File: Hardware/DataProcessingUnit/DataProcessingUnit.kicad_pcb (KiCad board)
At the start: 2 copper layers, 85 x 60 mm, 49 parts, among them J1 USB_B_Micro, J4 Conn_01x07, Q2 BC847, SW1 SW_Push, U2 LD1117S33TR, U3 STM32F103RBTx, Y1 32,768kHz, Y2 Crystal

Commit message: corections after hw sw integration
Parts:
- C11, C12: value 6p8 -> 10p
- C13, C14: value 6p8 -> 22p
- C9: value 100n -> 1u
- R13, R14: value TBD -> 0R
- Y1: value 32,768kHz -> 32,768kHz /12.5p
- Y2: value Crystal -> 8M
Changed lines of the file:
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@@
 			(psa4output no)
 			(plot_black_and_white yes)
-			(plotinvisibletext no)
 			(sketchpadsonfab no)
 			(plotpadnumbers no)
@@
 			)
 		)
-		(property "Value" "32,768kHz"
+		(property "Value" "32,768kHz /12.5p"
 			(at 0 2.000001 45)
 			(layer "F.Fab")
@@
 			)
 		)
-		(property "Value" "6p8"
+		(property "Value" "10p"
 			(at 0 1.679999 135)
 			(layer "F.Fab")
@@
 			)
 		)
-		(property "Value" "TBD"
+		(property "Value" "0R"
 			(at 0 1.65 45)
 			(layer "F.Fab")
@@
 			)
 		)
-		(property "Value" "TBD"
+		(property "Value" "0R"
 			(at 0 1.65 45)
 			(layer "F.Fab")
@@
 			)
 		)
-		(property "Value" "Crystal"
+		(property "Value" "8M"
 			(at 0 3.55 135)
 			(layer "F.Fab")
@@
 			)
 		)
-		(property "Value" "6p8"
+		(property "Value" "10p"
 			(at 0 1.679999 135)
 			(layer "F.Fab")
@@
 			)
 		)
-		(property "Value" "6p8"
+		(property "Value" "22p"
 			(at 0 1.679999 45)
 			(layer "F.Fab")
@@
 				(keep_text_aligned yes)
 			)
-			(gr_text "39,54"
+			(gr_text "39.54"
 				(at 192.27 129.15 0)
 				(layer "F.Fab")
@@
 				(keep_text_aligned yes)
 			)
-			(gr_text "79,5"
+			(gr_text "79.5"
 				(at 172.29 104.65 0)
 				(layer "User.1")
@@
 			)
 		)
-		(property "Value" "6p8"
+		(property "Value" "22p"
 			(at 0 1.679999 45)
 			(layer "F.Fab")
@@
 			)
 		)
-		(property "Value" "100n"
+		(property "Value" "1u"
 			(at 0 1.68 0)
 			(layer "F.Fab")
@@
 			(keep_text_aligned yes)
 		)
-		(gr_text "85,0000 mm"
+		(gr_text "85.0000 mm"
 			(at 172.5 126.35 0)
 			(layer "Cmts.User")
@@
 			(keep_text_aligned yes)
 		)
-		(gr_text "100,0000 mm"
+		(gr_text "100.0000 mm"
 			(at 124.6 70 90)
 			(layer "Cmts.User")
@@
 			(keep_text_aligned yes)
 		)
-		(gr_text "60,0000 mm"
+		(gr_text "60.0000 mm"
 			(at 223.85 90 90)
 			(layer "Cmts.User")
@@
 			(keep_text_aligned yes)
 		)
-		(gr_text "100,0000 mm"
+		(gr_text "100.0000 mm"
 			(at 180 133.85 0)
 			(layer "Cmts.User")
@@
 			(keep_text_aligned yes)
 		)
-		(gr_text "42,5000 mm"
+		(gr_text "42.5000 mm"
 			(at 151.25 122.2 0)
 			(layer "Cmts.User")

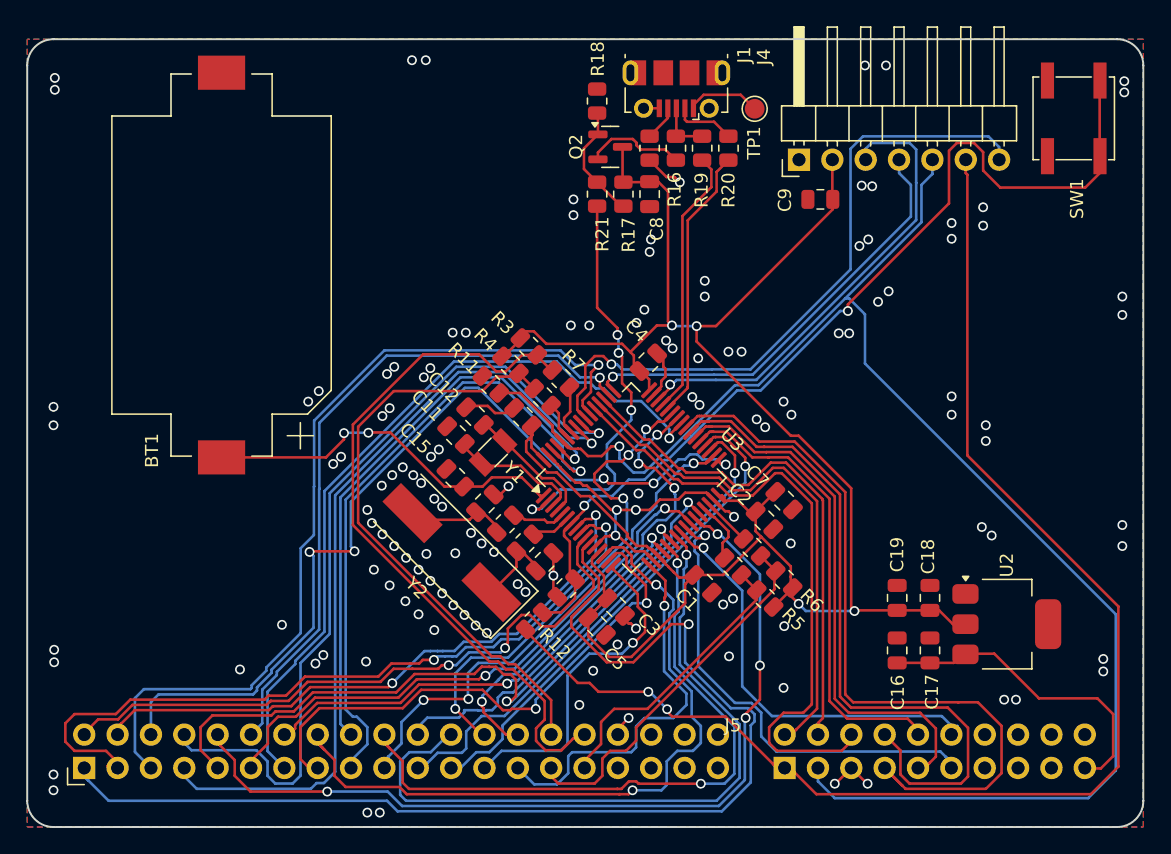
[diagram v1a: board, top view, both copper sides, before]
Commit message: rework CI, make PCB smaller
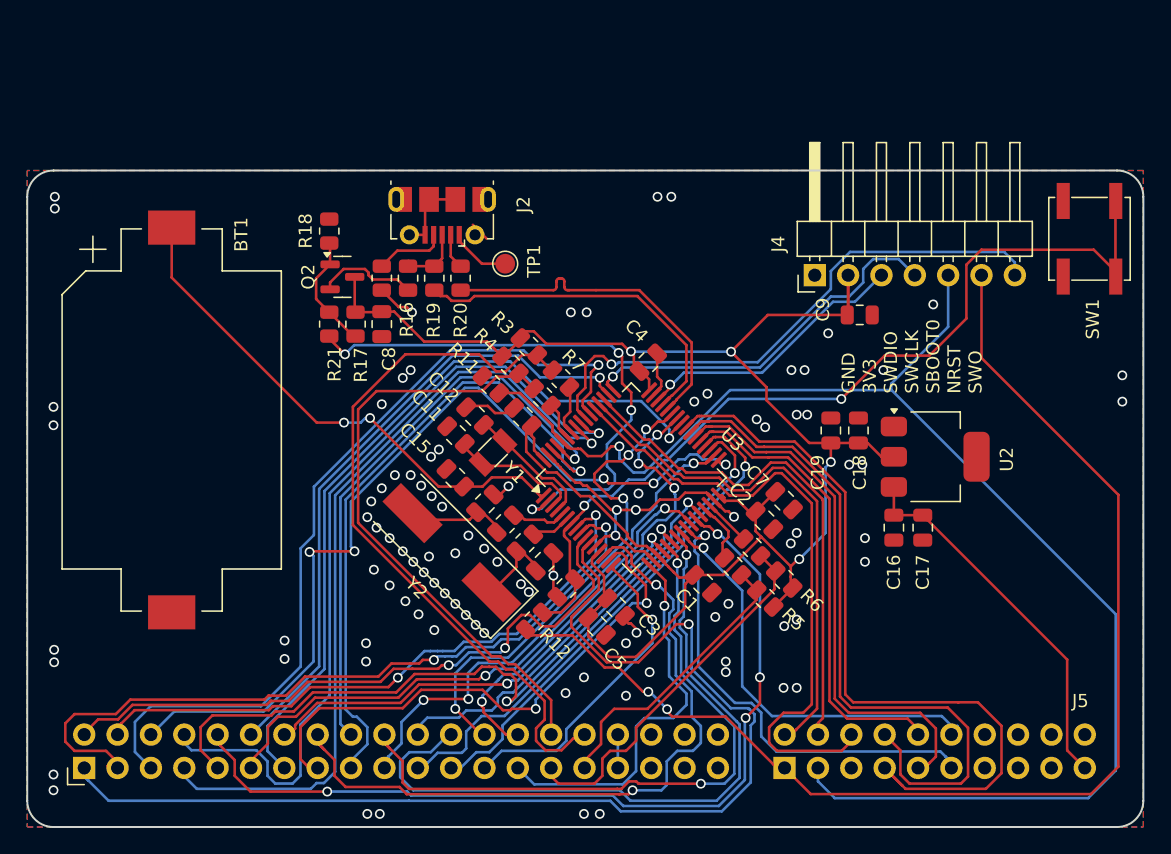
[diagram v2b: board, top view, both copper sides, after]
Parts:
- removed J1: USB_B_Micro, Connector_USB:USB_Micro-B_Molex-105017-0001
- added J2: USB_B_Micro, HardwareDataLogger:USB_Micro-B_Molex-105017-0001_Extra_Mechanical_Pads, F.Cu at (162.0, 75.7)
- C11, C12: value 10p -> 6p8
- C13, C14: value 22p -> 6p8
- C9: value 1u -> 100n
- R13, R14: value 0R -> TBD
- Y1: value 32,768kHz /12.5p -> 32,768kHz
- Y2: value 8M -> Crystal
- moved C8 22.7 mm to (157.0, 81.7)
- moved R15 22.7 mm to (157.0, 78.2)
- moved R16 22.7 mm to (159.0, 78.2)
- moved R17 22.7 mm to (155.0, 81.7)
- moved R19 22.7 mm to (161.0, 78.2)
- moved R20 22.7 mm to (163.0, 78.2)
- moved R21 22.7 mm to (153.0, 81.7)
- moved Q2 22.7 mm to (154.0, 78.1)
- moved R18 22.7 mm to (153.0, 74.6)
- moved TP1 22.4 mm to (166.4, 77.1)
- moved C18 13.9 mm to (193.3, 89.8)
- moved U2 13.9 mm to (199.2, 91.8)
- moved C19 13.7 mm to (191.2, 89.8)
- moved BT1 12.4 mm to (141.0, 89.0), turned to -90 degrees
- moved C17 9.37 mm to (198.2, 97.2), turned to -90 degrees
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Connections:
- net USB_DM renamed USB_N
- net USB_DP renamed USB_P
- J5 pad 35: 12V -> unconnected-(J5-Pin_35-Pad35)
- J5 pad 36: -12V -> unconnected-(J5-Pin_36-Pad36)
- J5 pad 37: 3V3_FROM_MAINBOARD -> unconnected-(J5-Pin_37-Pad37)
- J5 pad 38: -3V3 -> unconnected-(J5-Pin_38-Pad38)
- J5 pad 39: 5V -> unconnected-(J5-Pin_39-Pad39)
- J5 pad 40: -5V -> unconnected-(J5-Pin_40-Pad40)
- J5 pad 55: 12V -> unconnected-(J5-Pin_55-Pad55)
- J5 pad 56: -12V -> unconnected-(J5-Pin_56-Pad56)
- J5 pad 57: 3V3_FROM_MAINBOARD -> unconnected-(J5-Pin_57-Pad57)
- J5 pad 58: -3V3 -> unconnected-(J5-Pin_58-Pad58)
- J5 pad 60: -5V -> unconnected-(J5-Pin_60-Pad60)
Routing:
- net +3.3V: track 156.6 -> 140.2 mm
- net SYS_JTMS_SWDIO: track 35.9 -> 21.1 mm
- net Net-(BT1-+): track 28.2 -> 39.9 mm
- net /MCU/USB_ENUM: track 31.7 -> 42.9 mm
- net BOOT0: track 118.8 -> 108.0 mm
- net NRST: track 101.4 -> 93.0 mm
- net SWO: track 50.8 -> 43.4 mm
- net USB_P: track 20.4 -> 26.5 mm
- net USB_N: track 20.8 -> 26.4 mm
- net 5V: track 23.4 -> 28.7 mm
- net SYS_JTCK_SWCLK: track 33.1 -> 28.5 mm
- net Net-(U3-NRST): track 72.4 -> 68.0 mm
- net GND: track 45.9 -> 50.1 mm, vias 134 -> 97
- net GPIO_5: track 51.7 -> 48.8 mm
- net GPIO_12: track 66.1 -> 63.3 mm
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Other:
- board size 85 x 60 mm -> 85 x 50 mm
- board text added: "GND 3V3 SWDIO SWCLK SBOOT0 NRST SWO"
